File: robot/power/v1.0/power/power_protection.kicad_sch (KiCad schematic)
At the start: 33 parts, among them Q2 2N7002, Q3 BSC070N10NS5, Q4 BSC070N10NS5, Q5 MMBT5401LT1G, SW2 JST_SH, SW3 CPG151101D91, U4 LM5069, U5 LTC2955-2

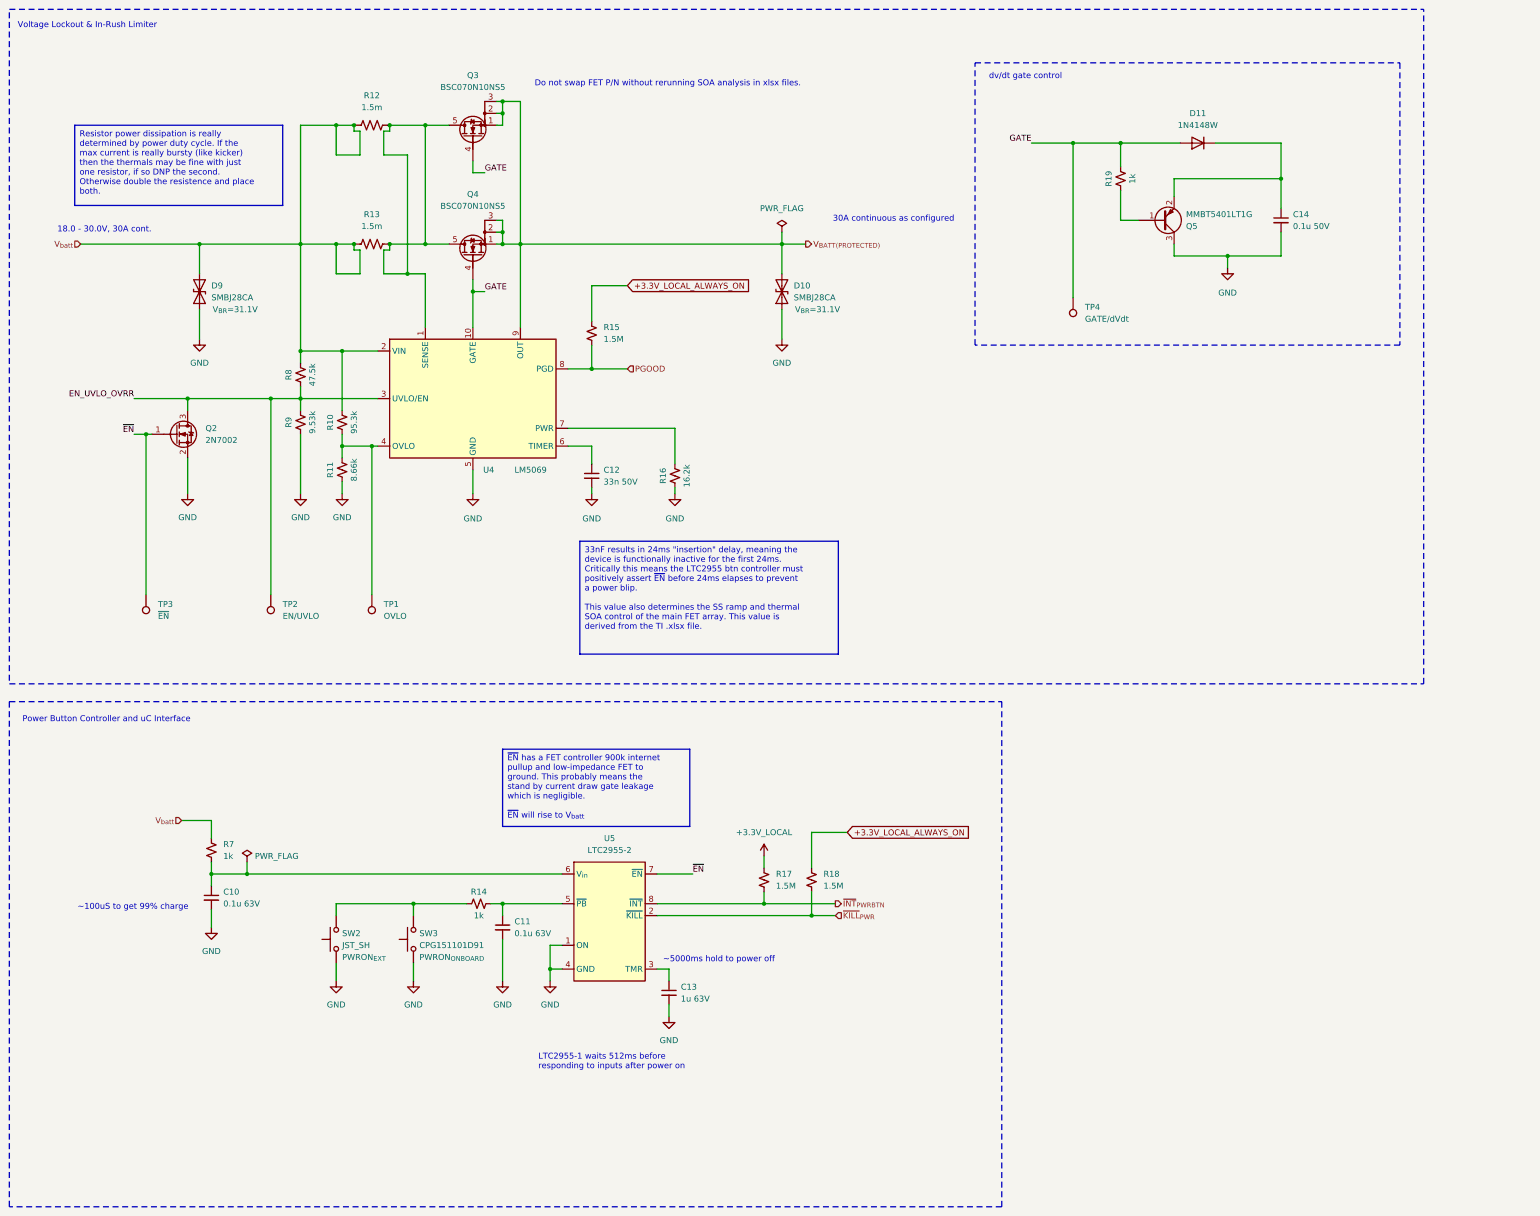
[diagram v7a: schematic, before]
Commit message: swap power fets
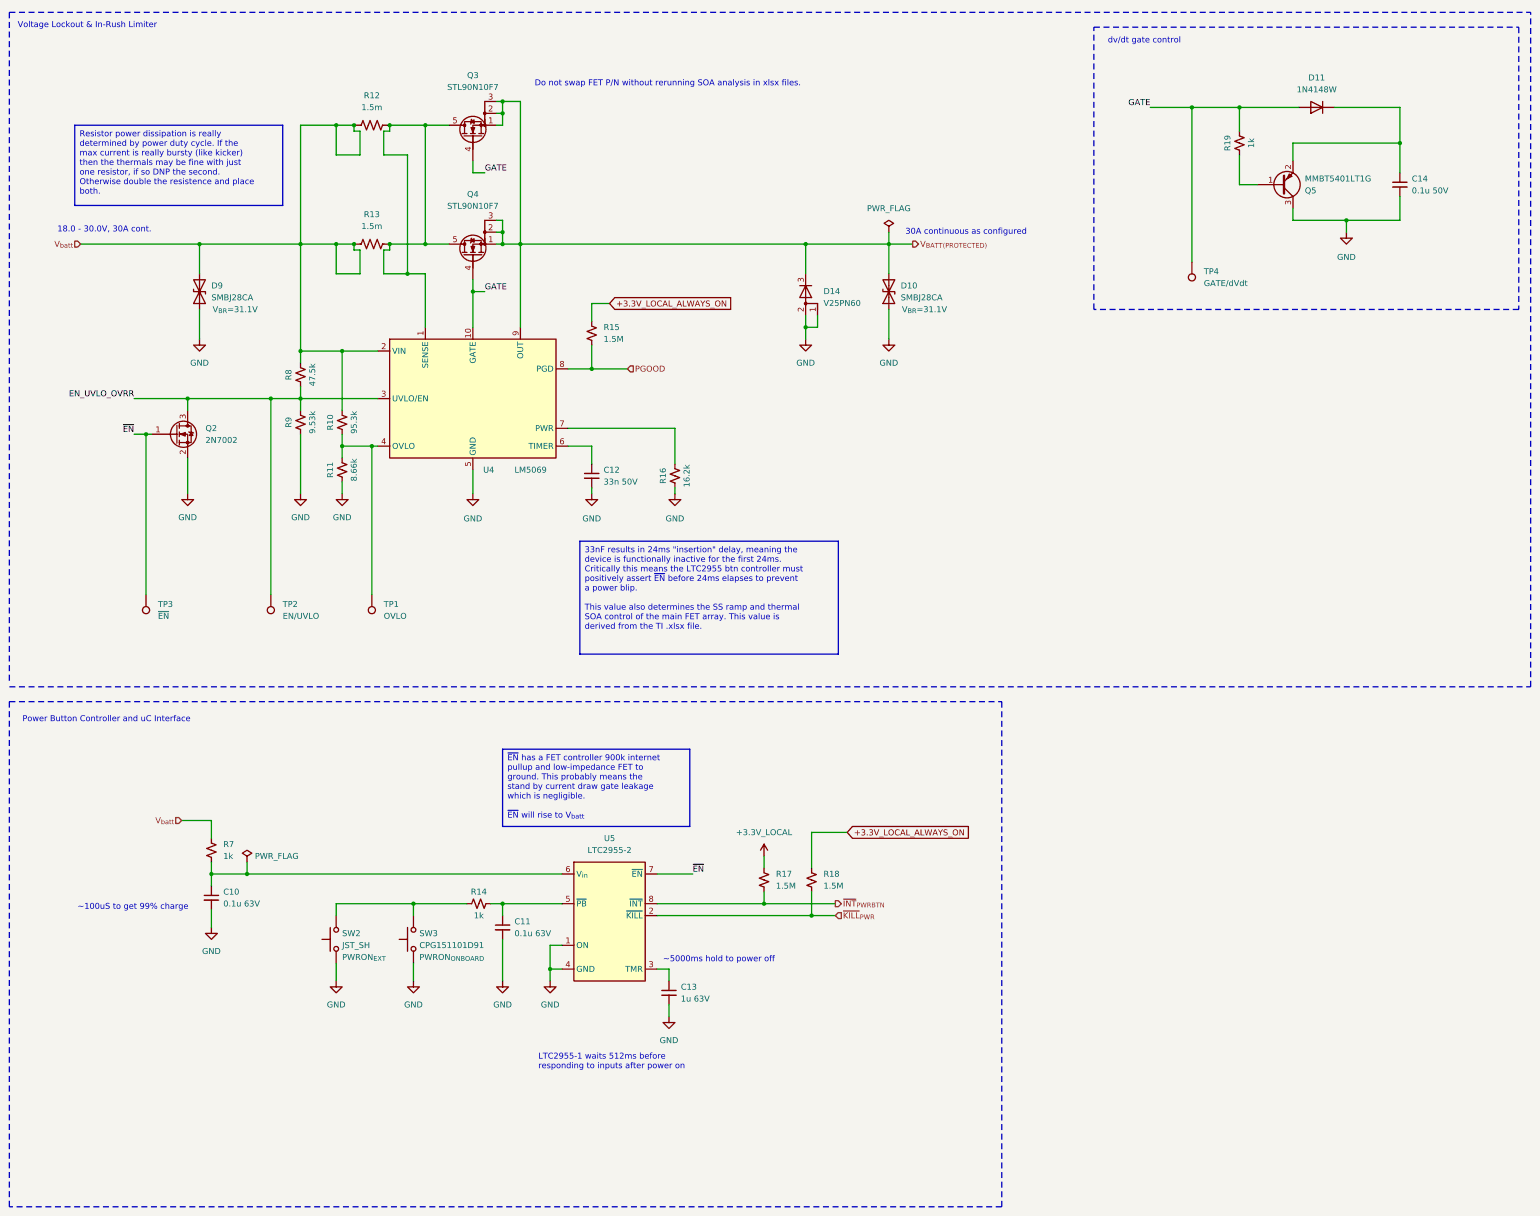
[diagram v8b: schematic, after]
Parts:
- added D14: V25PN60, Package_TO_SOT_SMD:TO-277A, symbol Device:D_AAK
- Q3, Q4: value BSC070N10NS5 -> STL90N10F7
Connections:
- net GND: now also D14.1 (A), D14.2 (A)
- net V_{BATT(PROTECTED)}: now also D14.3 (K)
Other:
- moved on the sheet: C14, D10, D11, Q5, R19, TP4
